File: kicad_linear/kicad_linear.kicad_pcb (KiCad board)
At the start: 2 copper layers, 25.4 x 28.8 mm, 7 parts, among them J1 latch, J3 PGM, J4 bus, U1 ATtiny1616-S, U2 HSN-3621

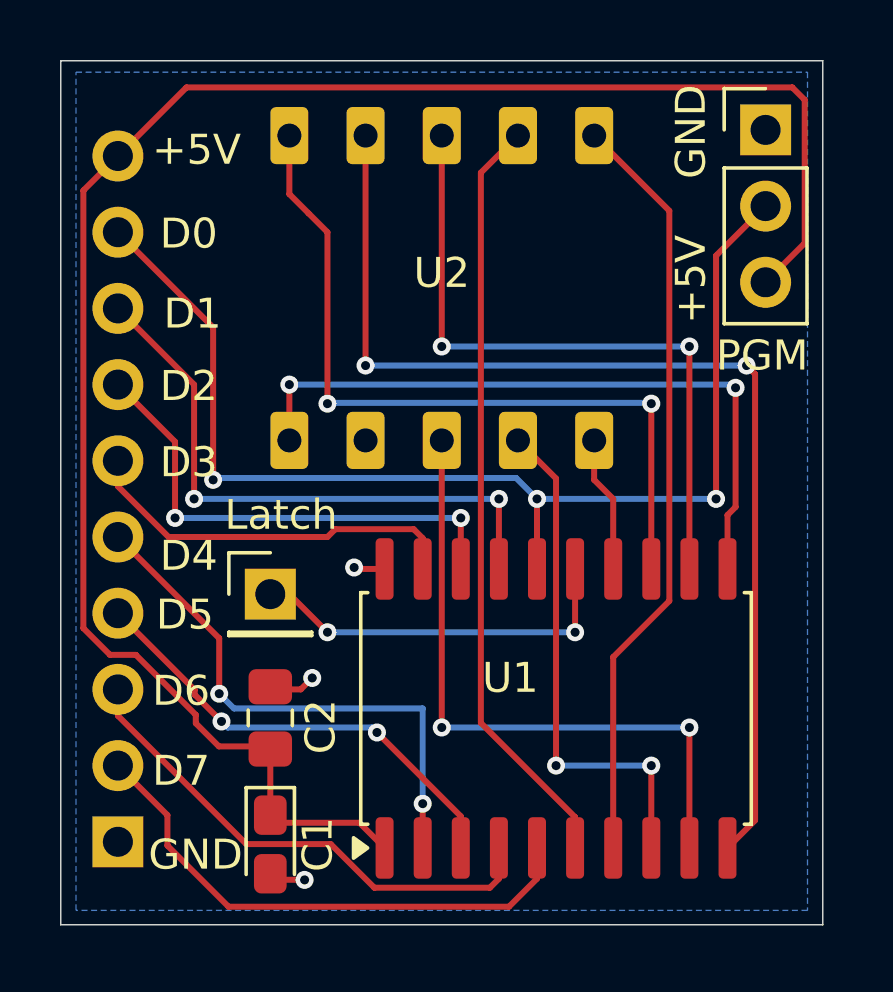
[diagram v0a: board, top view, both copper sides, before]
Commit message: Fix capacitor footprint
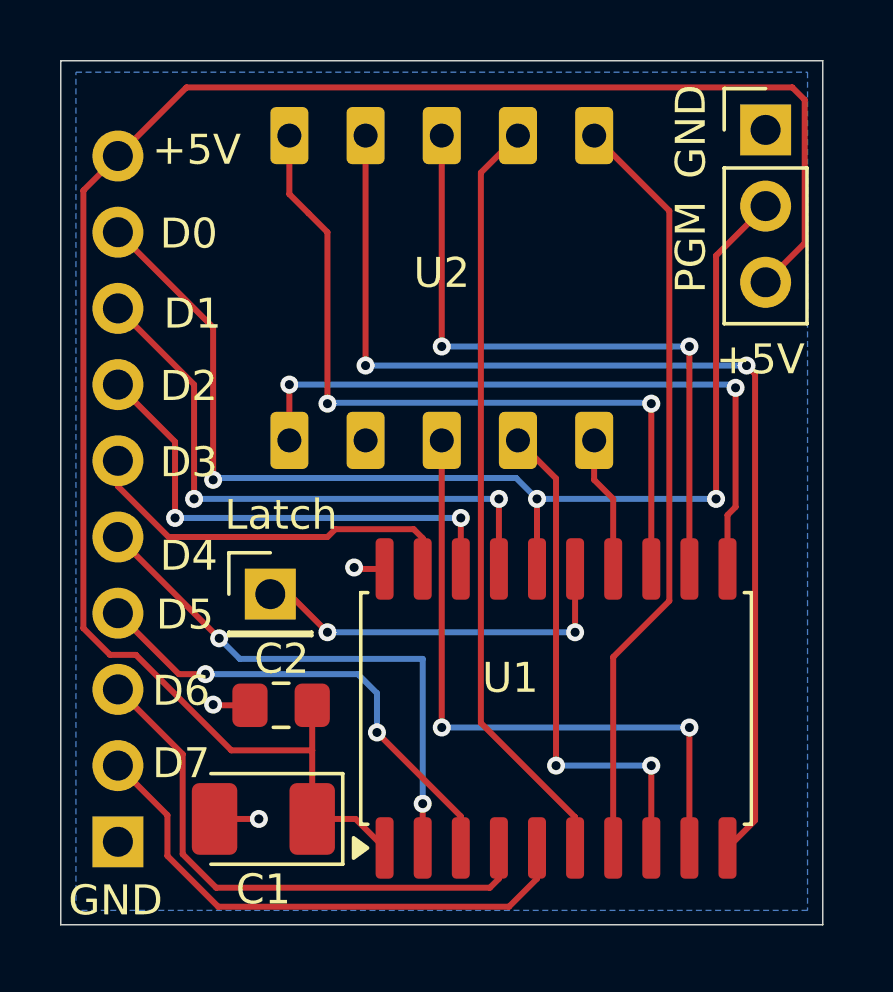
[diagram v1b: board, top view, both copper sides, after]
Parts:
- C1: footprint Capacitor_Tantalum_SMD:CP_EIA-2012-12_Kemet-R_HandSolder -> Capacitor_Tantalum_SMD:CP_EIA-3528-12_Kemet-T_HandSolder
- moved C1 0.88 mm to (133.8, 104.6), turned to 180 degrees
- moved C2 0.55 mm to (134.3, 100.9), turned to 180 degrees
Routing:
- net /D6: track 17.1 -> 18.5 mm
- net +5V: track 61.6 -> 62.8 mm
- net /D5: track 15.4 -> 16.1 mm
